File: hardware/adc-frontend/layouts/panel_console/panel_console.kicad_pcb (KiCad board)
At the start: 2 copper layers, 100 x 100 mm, 6 parts

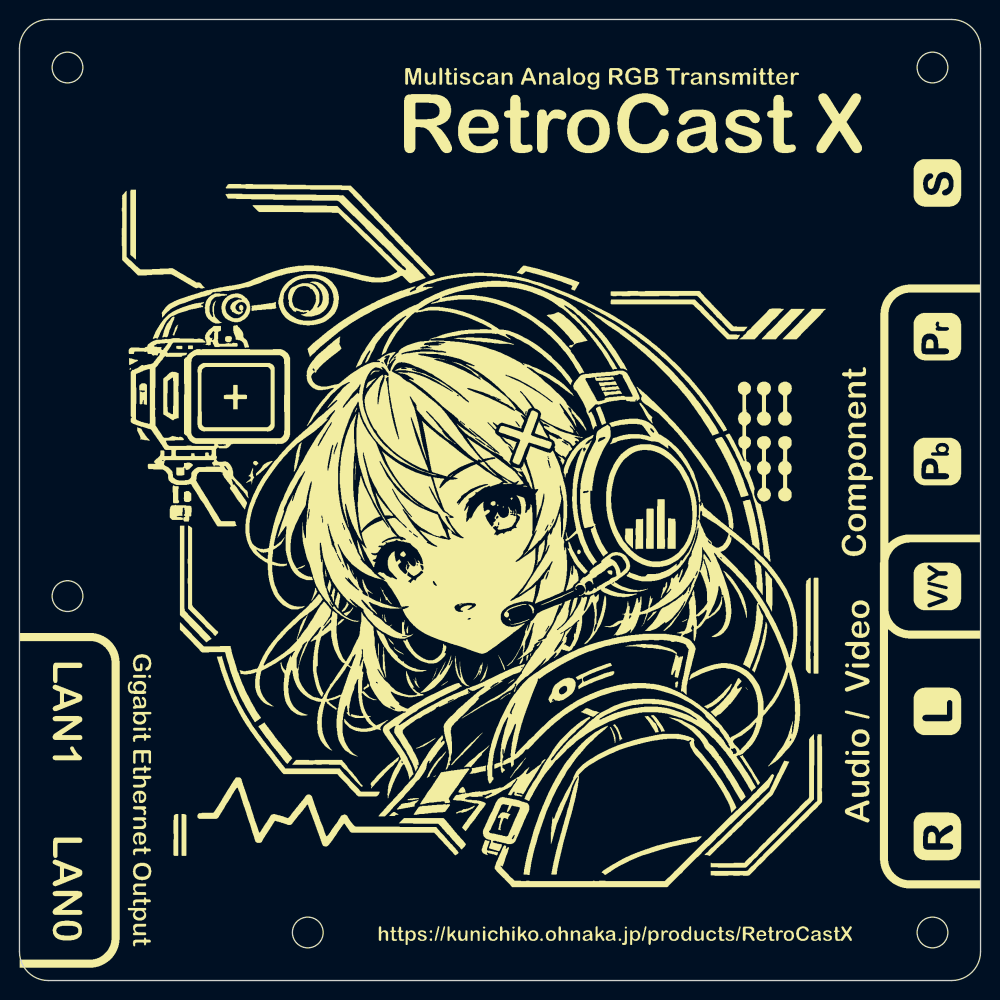
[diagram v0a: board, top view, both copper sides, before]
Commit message: パネルを GND シールドにし、メイン基板のシルクのはみ出しを直す
- パネル2枚: ネジ穴をメッキ穴 + φ6.4 GND パッドにし、表裏を GND で全面塗りつぶす。
  金属スペーサー・ネジで基板の取付穴(GND)とつなぎ、基板を挟む GND 面にする。
  製造データを v1.0.1 で出し直す(v1.0.0 は注文済みの銅箔なし版として残す)
- gen_panels.py / gen_panel_templates.py を上の内容に合わせる
- メイン基板: J1/J2/J8/J11/J12/J13 の基板外に出ていたシルクを F.Fab に移し、
  基板内の部分だけをシルクに残す。parts/ のフットプリントも同じに直す
  (製造データは次の注文時に出し直す)

Co-Authored-By: Claude Opus 5.5 (1M context) <noreply@anthropic.com>
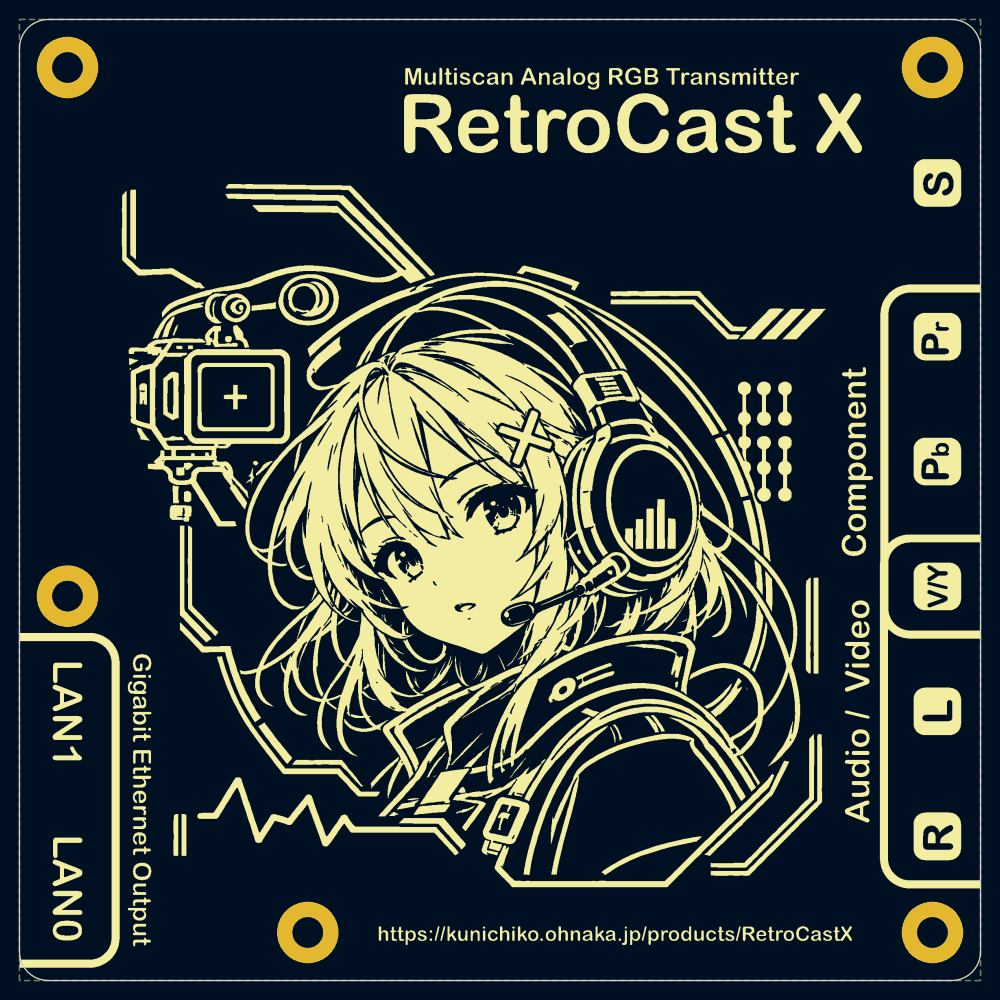
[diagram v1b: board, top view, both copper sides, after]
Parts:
- H1, H2, H3, H4, H5: value MountingHole_3.2mm_M3 -> MountingHole_3.2mm_M3_Pad; footprint MountingHole_3.2mm_M3 -> MountingHole_3.2mm_M3_Pad
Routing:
- added copper zone on B.Cu, net GND
- added copper zone on F.Cu, net GND
